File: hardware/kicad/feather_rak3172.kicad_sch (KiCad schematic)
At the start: 51 parts, among them J1 Pin Header, J2 Pin Header, J3 USB_C_Receptacle_USB2.0, J4 915MHz SMA, J5 SWD, J6 JST-2PH, Q1 DMG3415UQ-7, SW1 RESET, SW2 BOOT, U1 RAK3172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

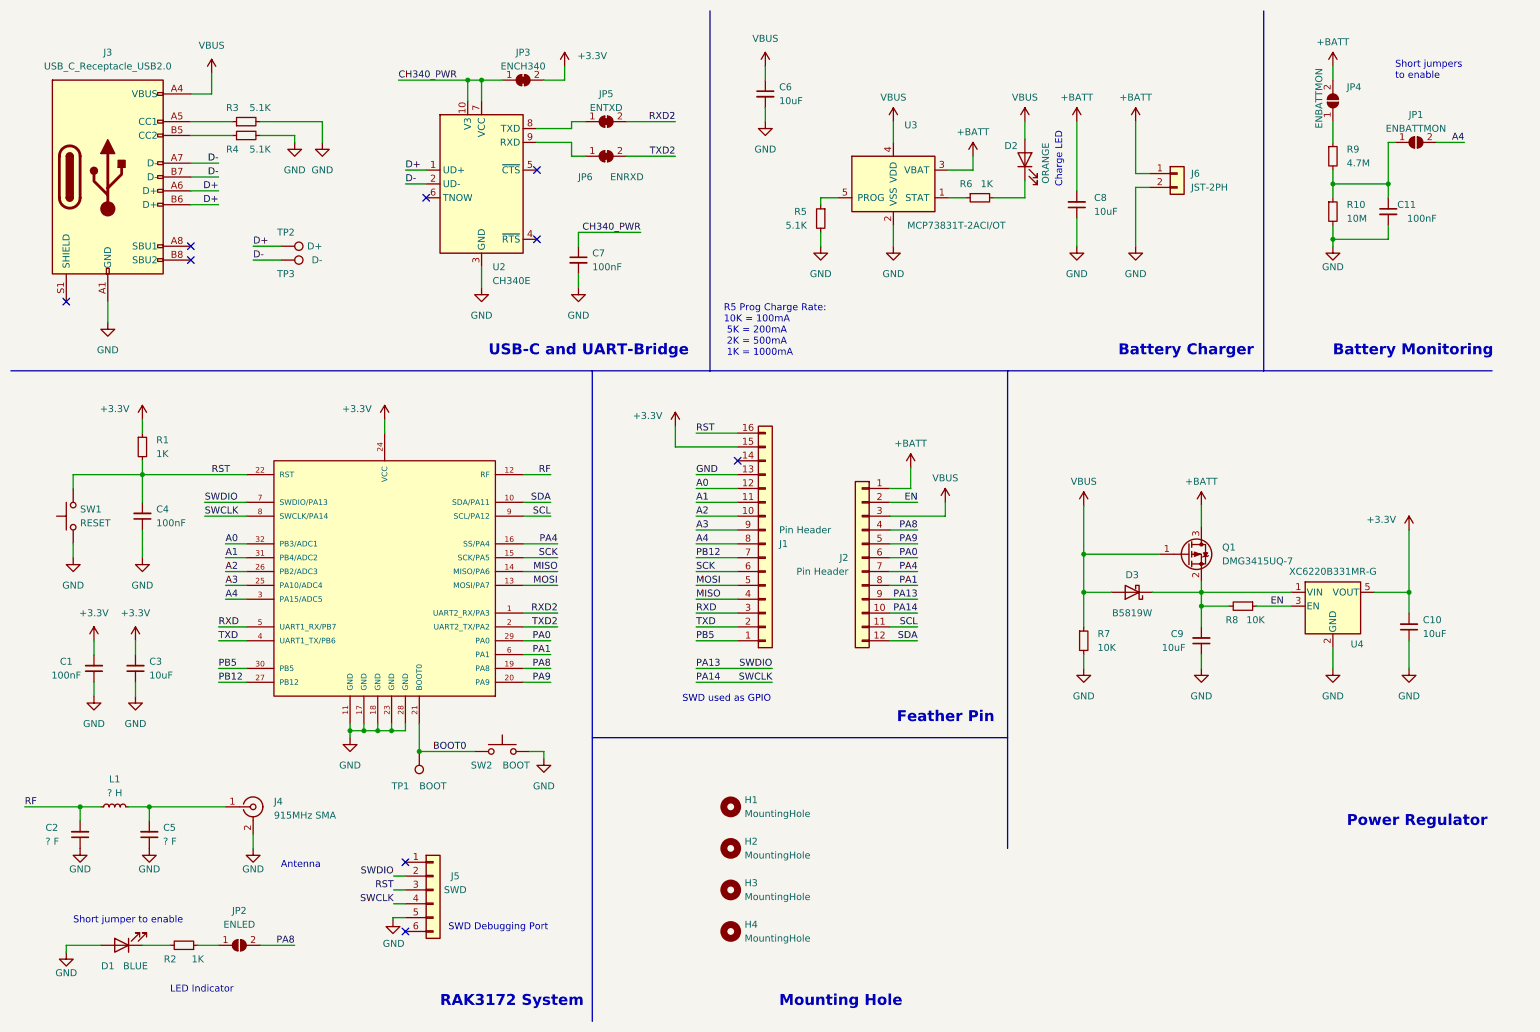
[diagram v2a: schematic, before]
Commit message: minor schematic unit changes
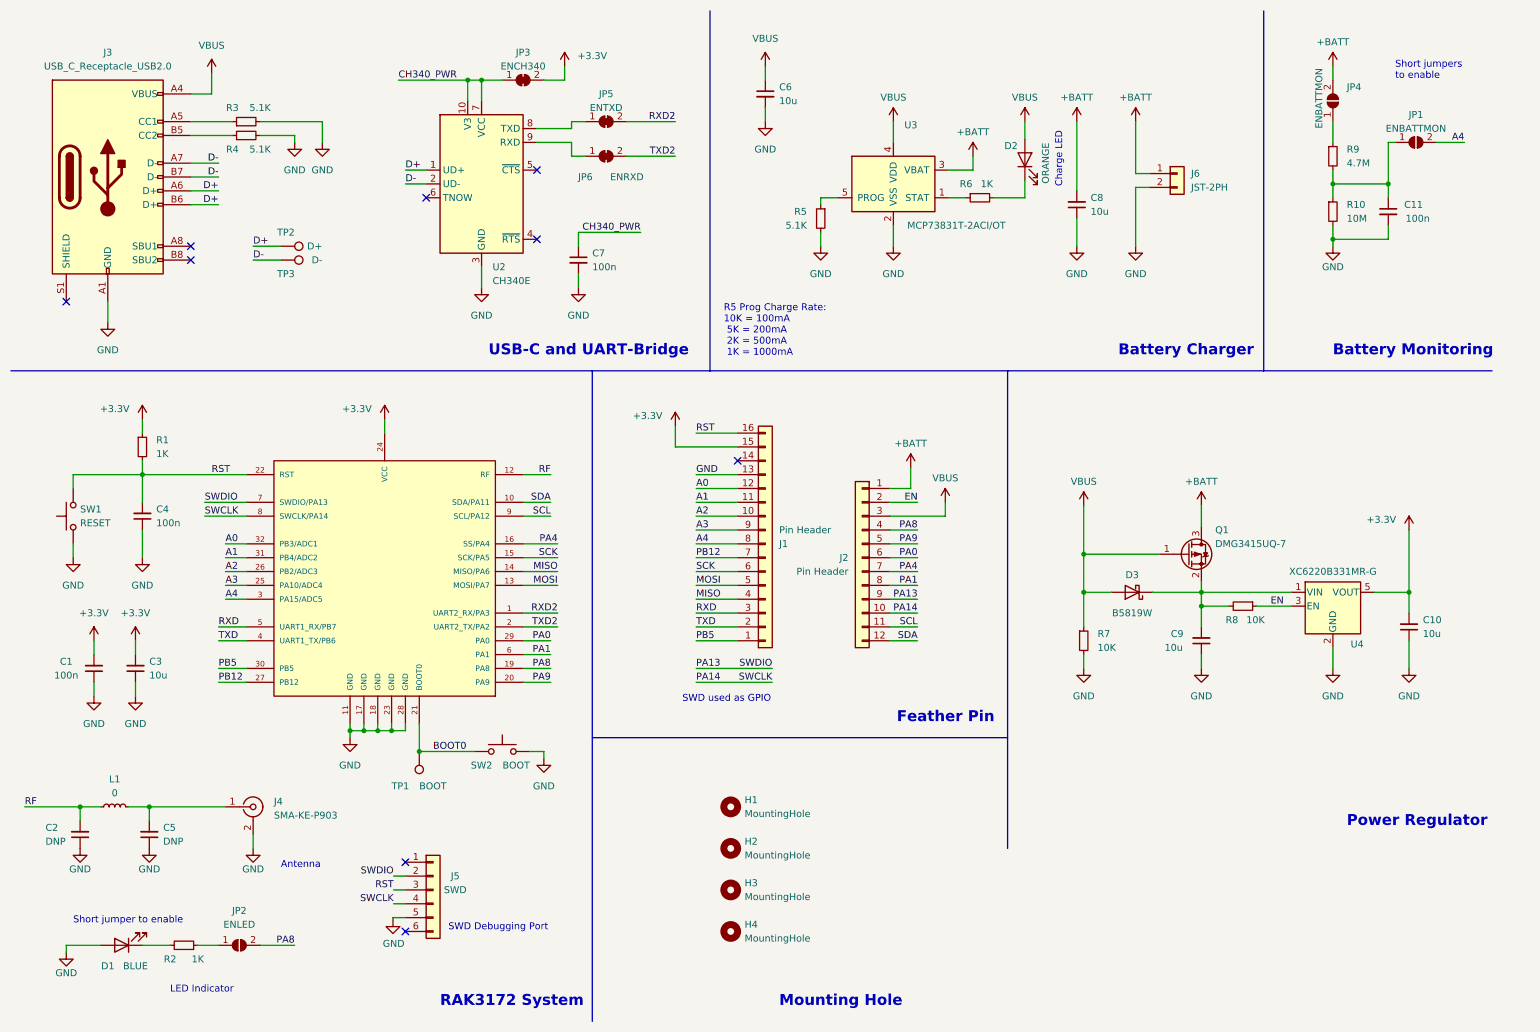
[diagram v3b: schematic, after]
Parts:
- C1, C11, C4, C7: value 100nF -> 100n
- C10, C3, C6, C8, C9: value 10uF -> 10u
- C2, C5: value ? F -> DNP
- J4: value 915MHz SMA -> SMA-KE-P903
- L1: value ? H -> 0
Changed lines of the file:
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@@
     (title "Feather RAK3172")
     (date "2023-03-20")
-    (rev "8.2")
+    (rev "8.3")
     (company "Teapot Laboratories")
   )
@@
       (effects (font (size 1.27 1.27)) (justify right))
     )
-    (property "Value" "? F" (id 1) (at 19.05 165.1 0)
+    (property "Value" "DNP" (id 1) (at 19.05 165.1 0)
       (effects (font (size 1.27 1.27)) (justify right))
     )
@@
     (in_bom yes) (on_board yes)
     (property "Reference" "C1" (id 0) (at 22.86 132.08 0))
-    (property "Value" "100nF" (id 1) (at 22.86 134.62 0))
+    (property "Value" "100n" (id 1) (at 22.86 134.62 0))
     (property "Footprint" "Capacitor_SMD:C_0603_1608Metric" (id 2) (at 27.94 133.35 0)
       (effects (font (size 1.27 1.27)) hide)
@@
       (effects (font (size 1.27 1.27)) (justify left))
     )
-    (property "Value" "100nF" (id 1) (at 119.38 59.6962 0)
+    (property "Value" "100n" (id 1) (at 119.38 59.6962 0)
       (effects (font (size 1.27 1.27)) (justify left))
     )
@@
     (in_bom yes) (on_board yes)
     (property "Reference" "L1" (id 0) (at 31.75 153.67 90))
-    (property "Value" "? H" (id 1) (at 31.75 156.21 90))
+    (property "Value" "0" (id 1) (at 31.75 156.21 90))
     (property "Footprint" "Inductor_SMD:L_0402_1005Metric" (id 2) (at 31.75 158.75 0)
       (effects (font (size 1.27 1.27)) hide)
@@
   (symbol (lib_id "Device:C_Small") (at 265.43 49.53 0) (unit 1)
     (in_bom yes) (on_board yes)
-    (property "Reference" "C11" (id 0) (at 270.51 48.26 0)
+    (property "Reference" "C11" (id 0) (at 271.78 48.26 0)
       (effects (font (size 1.27 1.27)) (justify right))
     )
-    (property "Value" "100nF" (id 1) (at 274.32 50.8 0)
+    (property "Value" "100n" (id 1) (at 273.05 50.8 0)
       (effects (font (size 1.27 1.27)) (justify right))
     )
@@
       (effects (font (size 1.27 1.27)) (justify left))
     )
-    (property "Value" "915MHz SMA" (id 1) (at 60.96 160.3131 0)
+    (property "Value" "SMA-KE-P903" (id 1) (at 60.96 160.3131 0)
       (effects (font (size 1.27 1.27)) (justify left))
     )
@@
       (effects (font (size 1.27 1.27)) (justify right))
     )
-    (property "Value" "10uF" (id 1) (at 271.78 126.9935 0)
+    (property "Value" "10u" (id 1) (at 271.78 126.9935 0)
       (effects (font (size 1.27 1.27)) (justify right))
     )
@@
   )
   (symbol (lib_id "Device:Q_PMOS_GSD") (at 228.6 112.395 0) (unit 1)
-    (in_bom yes) (on_board yes) (fields_autoplaced)
-    (property "Reference" "Q1" (id 0) (at 234.95 111.1249 0)
-      (effects (font (size 1.27 1.27)) (justify left))
-    )
-    (property "Value" "DMG3415UQ-7" (id 1) (at 234.95 113.6649 0)
+    (in_bom yes) (on_board yes)
+    (property "Reference" "Q1" (id 0) (at 233.68 107.95 0)
+      (effects (font (size 1.27 1.27)) (justify left))
+    )
+    (property "Value" "DMG3415UQ-7" (id 1) (at 233.68 110.49 0)
       (effects (font (size 1.27 1.27)) (justify left))
     )
@@
       (effects (font (size 1.27 1.27)) (justify right))
     )
-    (property "Value" "? F" (id 1) (at 40.64 165.0935 0)
+    (property "Value" "DNP" (id 1) (at 40.64 165.0935 0)
       (effects (font (size 1.27 1.27)) (justify right))
     )
@@
       (effects (font (size 1.27 1.27)) (justify right))
     )
-    (property "Value" "100nF" (id 1) (at 39.37 106.6735 0)
+    (property "Value" "100n" (id 1) (at 39.37 106.6735 0)
       (effects (font (size 1.27 1.27)) (justify right))
     )
@@
       (effects (font (size 1.27 1.27)) (justify left))
     )
-    (property "Value" "10uF" (id 1) (at 153.67 29.2162 0)
+    (property "Value" "10u" (id 1) (at 153.67 29.2162 0)
       (effects (font (size 1.27 1.27)) (justify left))
     )
@@
       (effects (font (size 1.27 1.27)) (justify right))
     )
-    (property "Value" "10uF" (id 1) (at 38.1 134.6135 0)
+    (property "Value" "10u" (id 1) (at 38.1 134.6135 0)
       (effects (font (size 1.27 1.27)) (justify right))
     )
@@
   (symbol (lib_id "Device:C_Small") (at 208.28 48.26 180) (unit 1)
     (in_bom yes) (on_board yes) (fields_autoplaced)
-    (property "Reference" "C8" (id 0) (at 211.455 46.9835 0)
+    (property "Reference" "C8" (id 0) (at 210.82 46.9835 0)
       (effects (font (size 1.27 1.27)) (justify right))
     )
-    (property "Value" "10uF" (id 1) (at 211.455 49.5235 0)
+    (property "Value" "10u" (id 1) (at 210.82 49.5235 0)
       (effects (font (size 1.27 1.27)) (justify right))
     )
@@
     (in_bom yes) (on_board yes)
     (property "Reference" "C9" (id 0) (at 226.695 127 0))
-    (property "Value" "10uF" (id 1) (at 226.06 129.54 0))
+    (property "Value" "10u" (id 1) (at 226.06 129.54 0))
     (property "Footprint" "Capacitor_SMD:C_0805_2012Metric" (id 2) (at 231.14 128.27 0)
       (effects (font (size 1.27 1.27)) hide)
@@
     )
     (path "/114e503f-0fbb-4252-b9ed-9d13490a51d0"
-      (reference "C1") (unit 1) (value "100nF") (footprint "Capacitor_SMD:C_0603_1608Metric")
+      (reference "C1") (unit 1) (value "100n") (footprint "Capacitor_SMD:C_0603_1608Metric")
     )
     (path "/046872a0-329d-485e-bdbc-a4be053ebf6e"
-      (reference "C2") (unit 1) (value "? F") (footprint "Capacitor_SMD:C_0402_1005Metric")
+      (reference "C2") (unit 1) (value "DNP") (footprint "Capacitor_SMD:C_0402_1005Metric")
     )
     (path "/d711cacb-2e1b-475f-abfa-4a39a9e8f79f"
-      (reference "C3") (unit 1) (value "10uF") (footprint "Capacitor_SMD:C_0603_1608Metric")
+      (reference "C3") (unit 1) (value "10u") (footprint "Capacitor_SMD:C_0603_1608Metric")
     )
     (path "/a307f16f-34c0-49b8-8d92-f98047b85531"
-      (reference "C4") (unit 1) (value "100nF") (footprint "Capacitor_SMD:C_0603_1608Metric")
+      (reference "C4") (unit 1) (value "100n") (footprint "Capacitor_SMD:C_0603_1608Metric")
     )
     (path "/9d049245-a4a8-413a-ad83-e86b520dcd36"
-      (reference "C5") (unit 1) (value "? F") (footprint "Capacitor_SMD:C_0402_1005Metric")
+      (reference "C5") (unit 1) (value "DNP") (footprint "Capacitor_SMD:C_0402_1005Metric")
     )
     (path "/a3bb1d8b-acfd-4759-bb6f-6cb5578fa3b3"
-      (reference "C6") (unit 1) (value "10uF") (footprint "Capacitor_SMD:C_0603_1608Metric")
+      (reference "C6") (unit 1) (value "10u") (footprint "Capacitor_SMD:C_0603_1608Metric")
     )
     (path "/2b39d5ae-7698-42b2-918d-a4658a166a02"
-      (reference "C7") (unit 1) (value "100nF") (footprint "Capacitor_SMD:C_0603_1608Metric")
+      (reference "C7") (unit 1) (value "100n") (footprint "Capacitor_SMD:C_0603_1608Metric")
     )
     (path "/e6069698-a69c-4abc-b585-45d07d82eab0"
-      (reference "C8") (unit 1) (value "10uF") (footprint "Capacitor_SMD:C_0805_2012Metric")
+      (reference "C8") (unit 1) (value "10u") (footprint "Capacitor_SMD:C_0805_2012Metric")
     )
     (path "/ef0bf128-a477-4d2c-8597-03d909a6974d"
-      (reference "C9") (unit 1) (value "10uF") (footprint "Capacitor_SMD:C_0805_2012Metric")
+      (reference "C9") (unit 1) (value "10u") (footprint "Capacitor_SMD:C_0805_2012Metric")
     )
     (path "/93db649d-df3b-46fd-9801-8bc0e049284b"
-      (reference "C10") (unit 1) (value "10uF") (footprint "Capacitor_SMD:C_0805_2012Metric")
+      (reference "C10") (unit 1) (value "10u") (footprint "Capacitor_SMD:C_0805_2012Metric")
     )
     (path "/67d033e9-1e89-40b4-8152-d4a6964fae39"
-      (reference "C11") (unit 1) (value "100nF") (footprint "Capacitor_SMD:C_0603_1608Metric")
+      (reference "C11") (unit 1) (value "100n") (footprint "Capacitor_SMD:C_0603_1608Metric")
     )
     (path "/38de6b57-4abe-48ed-b377-c672334ba149"
@@
     )
     (path "/6d4b0e6f-888b-4ffe-a917-57f63f8b803a"
-      (reference "J4") (unit 1) (value "915MHz SMA") (footprint "Teapot:SMA_HJTech_023")
+      (reference "J4") (unit 1) (value "SMA-KE-P903") (footprint "Teapot:SMA_HJTech_023")
     )
     (path "/f936ce53-948e-44b1-9dff-b7868ae44450"
@@
     )
     (path "/2f732801-c0be-4b76-a61d-002040a3c720"
-      (reference "L1") (unit 1) (value "? H") (footprint "Inductor_SMD:L_0402_1005Metric")
+      (reference "L1") (unit 1) (value "0") (footprint "Inductor_SMD:L_0402_1005Metric")
     )
     (path "/9a62f1db-3067-412f-b29a-937b11e855ce"

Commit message: fix components position
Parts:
- J4: footprint Teapot:SMA_HJTech_023 -> Teapot:SMA-KE-P903
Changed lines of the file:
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@@
     (title "Feather RAK3172")
     (date "2023-03-20")
-    (rev "8.3")
+    (rev "8.4")
     (company "Teapot Laboratories")
   )
@@
       (effects (font (size 1.27 1.27)) (justify left))
     )
-    (property "Footprint" "Teapot:SMA_HJTech_023" (id 2) (at 57.15 158.75 0)
+    (property "Footprint" "Teapot:SMA-KE-P903" (id 2) (at 57.15 158.75 0)
       (effects (font (size 1.27 1.27)) hide)
     )
@@
     )
     (path "/6d4b0e6f-888b-4ffe-a917-57f63f8b803a"
-      (reference "J4") (unit 1) (value "SMA-KE-P903") (footprint "Teapot:SMA_HJTech_023")
+      (reference "J4") (unit 1) (value "SMA-KE-P903") (footprint "Teapot:SMA-KE-P903")
     )
     (path "/f936ce53-948e-44b1-9dff-b7868ae44450"

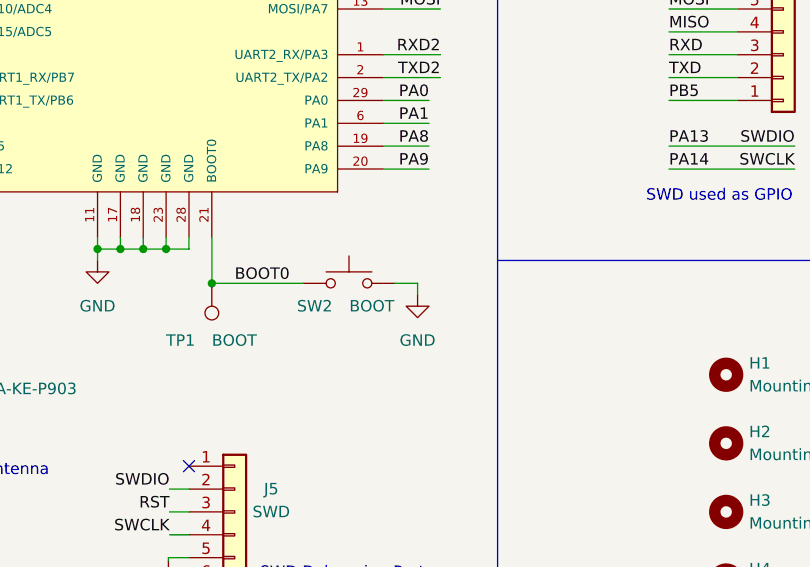
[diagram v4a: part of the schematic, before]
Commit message: change boot button to 3v3
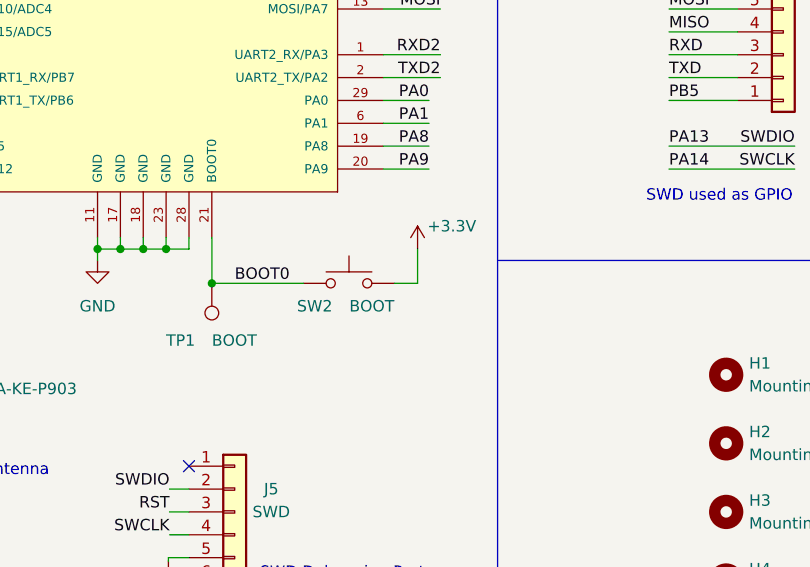
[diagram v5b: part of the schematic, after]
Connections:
- net +3.3V: now also SW2.1
- net BOOT0: now also SW2.2; no longer SW2.1
- net GND: no longer SW2.2
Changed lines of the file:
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@@
   (title_block
     (title "Feather RAK3172")
-    (date "2023-03-20")
-    (rev "8.4")
+    (date "2023-03-21")
+    (rev "9")
     (company "Teapot Laboratories")
   )
@@
     (stroke (width 0) (type default) (color 0 0 0 0))
   )
-  (wire (pts (xy 110.49 148.59) (xy 110.49 149.86))
-    (stroke (width 0) (type default) (color 0 0 0 0))
-  )
   (wire (pts (xy 45.72 33.02) (xy 53.34 33.02))
     (stroke (width 0) (type default) (color 0 0 0 0))
@@
   )
   (wire (pts (xy 106.68 125.73) (xy 113.03 125.73))
+    (stroke (width 0) (type default) (color 0 0 0 0))
+  )
+  (wire (pts (xy 110.49 144.78) (xy 110.49 148.59))
     (stroke (width 0) (type default) (color 0 0 0 0))
   )
@@
     )
   )
-  (symbol (lib_id "power:GND") (at 110.49 149.86 0) (unit 1)
-    (in_bom yes) (on_board yes)
-    (property "Reference" "#PWR0116" (id 0) (at 110.49 156.21 0)
-      (effects (font (size 1.27 1.27)) hide)
-    )
-    (property "Value" "GND" (id 1) (at 110.49 154.94 0))
-    (property "Footprint" "" (id 2) (at 110.49 149.86 0)
-      (effects (font (size 1.27 1.27)) hide)
-    )
-    (property "Datasheet" "" (id 3) (at 110.49 149.86 0)
-      (effects (font (size 1.27 1.27)) hide)
-    )
-    (pin "1")
-  )
-  (symbol (lib_id "Switch:SW_Push") (at 102.87 148.59 0) (unit 1)
+  (symbol (lib_id "Switch:SW_Push") (at 102.87 148.59 0) (mirror y) (unit 1)
     (in_bom yes) (on_board yes)
     (property "Reference" "SW2" (id 0) (at 99.06 151.13 0))
@@
     (pin "2")
   )
+  (symbol (lib_id "power:+3.3V") (at 110.49 144.78 0) (mirror y) (unit 1)
+    (in_bom yes) (on_board yes)
+    (property "Reference" "#PWR0116" (id 0) (at 110.49 148.59 0)
+      (effects (font (size 1.27 1.27)) hide)
+    )
+    (property "Value" "+3.3V" (id 1) (at 114.3 142.24 0))
+    (property "Footprint" "" (id 2) (at 110.49 144.78 0)
+      (effects (font (size 1.27 1.27)) hide)
+    )
+    (property "Datasheet" "" (id 3) (at 110.49 144.78 0)
+      (effects (font (size 1.27 1.27)) hide)
+    )
+    (pin "1")
+  )
   (symbol (lib_id "power:GND") (at 35.56 138.43 0) (unit 1)
     (in_bom yes) (on_board yes) (fields_autoplaced)
@@
       (reference "#PWR0115") (unit 1) (value "GND") (footprint "")
     )
-    (path "/0e43ed8b-5107-4d1f-b61a-7b930bf7de3d"
-      (reference "#PWR0116") (unit 1) (value "GND") (footprint "")
+    (path "/da66158f-be0b-4404-b194-6647f2c7c839"
+      (reference "#PWR0116") (unit 1) (value "+3.3V") (footprint "")
     )
     (path "/df66e71a-8d86-4126-bece-f6e459eabbe9"

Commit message: minor schematic changes
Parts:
- J1, J2: value Pin Header -> DNP
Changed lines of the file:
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@@
       (effects (font (size 1.27 1.27)) (justify left))
     )
-    (property "Value" "Pin Header" (id 1) (at 153.67 107.9501 0)
+    (property "Value" "DNP" (id 1) (at 153.67 107.9501 0)
       (effects (font (size 1.27 1.27)) (justify left))
     )
@@
       (effects (font (size 1.27 1.27)) (justify left))
     )
-    (property "Value" "Pin Header" (id 1) (at 166.37 115.5699 0)
+    (property "Value" "DNP" (id 1) (at 166.37 115.5699 0)
       (effects (font (size 1.27 1.27)) (justify left))
     )
@@
     )
     (path "/d6b41ed7-e99d-4609-b23a-95b1b5eb83ea"
-      (reference "J1") (unit 1) (value "Pin Header") (footprint "Connector_PinHeader_2.54mm:PinHeader_1x16_P2.54mm_Vertical")
+      (reference "J1") (unit 1) (value "DNP") (footprint "Connector_PinHeader_2.54mm:PinHeader_1x16_P2.54mm_Vertical")
     )
     (path "/f2d89196-a7c9-4b41-b283-223a8d7fdfe8"
-      (reference "J2") (unit 1) (value "Pin Header") (footprint "Connector_PinHeader_2.54mm:PinHeader_1x12_P2.54mm_Vertical")
+      (reference "J2") (unit 1) (value "DNP") (footprint "Connector_PinHeader_2.54mm:PinHeader_1x12_P2.54mm_Vertical")
     )
     (path "/9ecef5fe-9566-4045-9671-419d9c3abcc8"
